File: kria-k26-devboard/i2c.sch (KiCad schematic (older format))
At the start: 10 parts

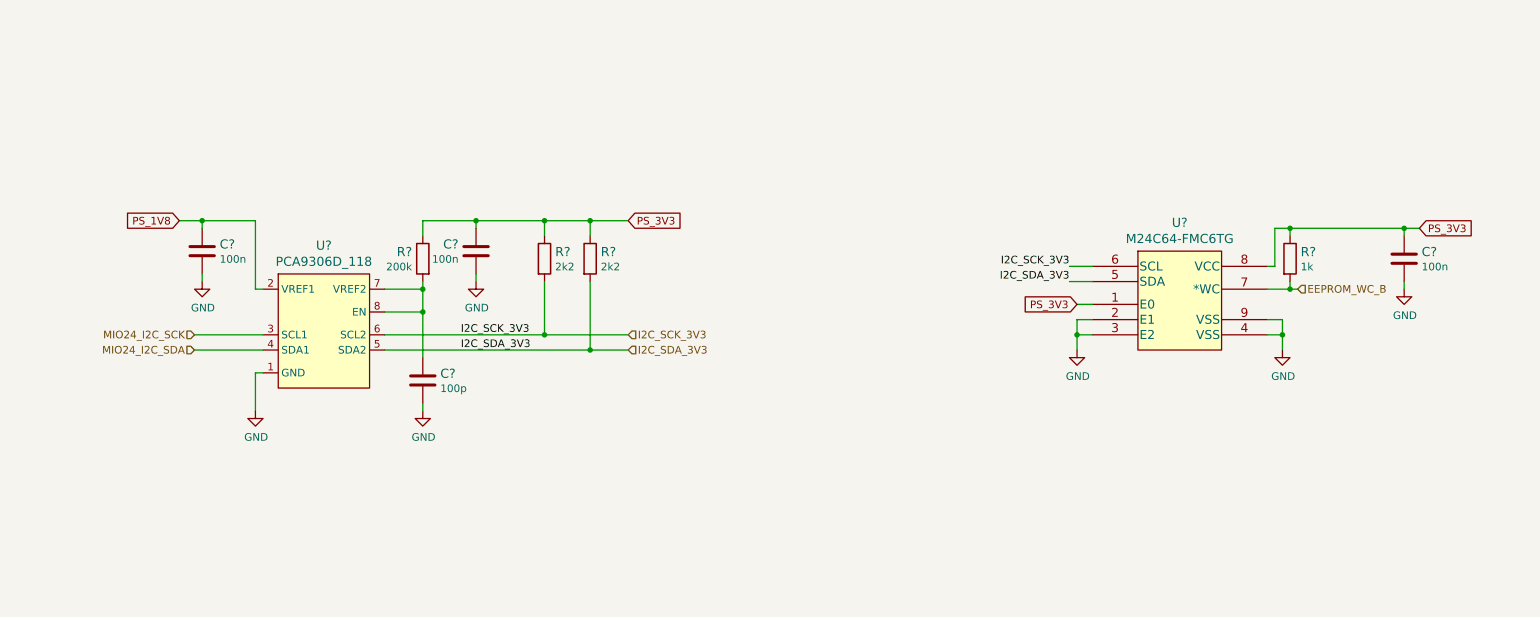
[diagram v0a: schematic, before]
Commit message: Added second ETH interface, connect POE PSE
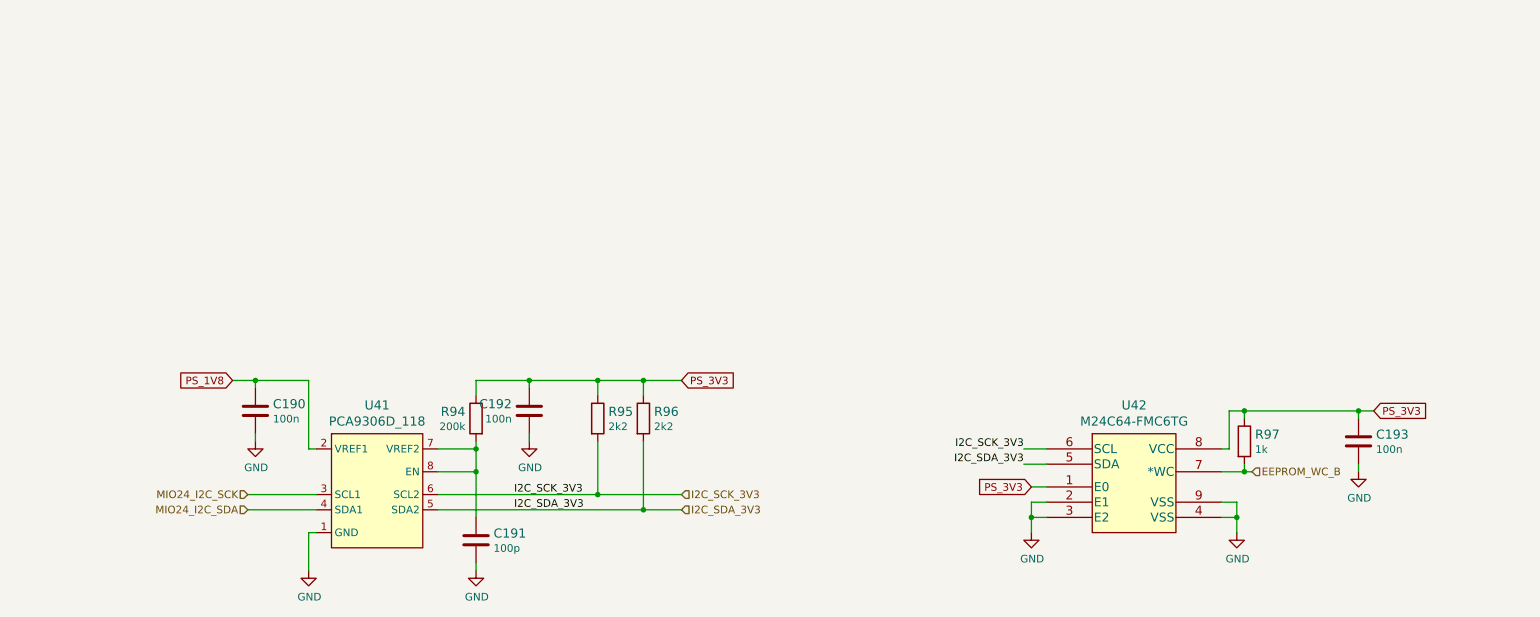
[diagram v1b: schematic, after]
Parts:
- gave numbers to parts that had none: 10
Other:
- moved on the sheet: C190, C191, C192, C193, R94, R95, R96, R97, U41, U42

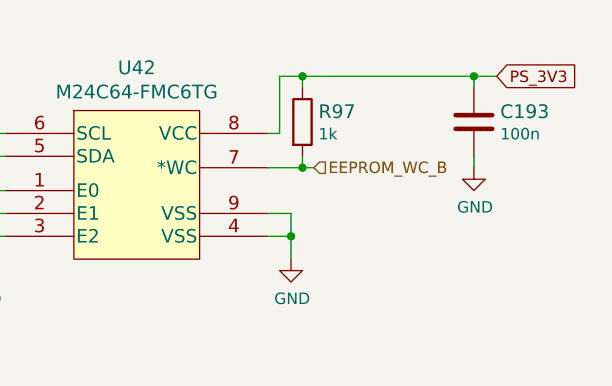
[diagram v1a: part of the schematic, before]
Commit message: Fixes on Reset pagae, progress through clock sheet
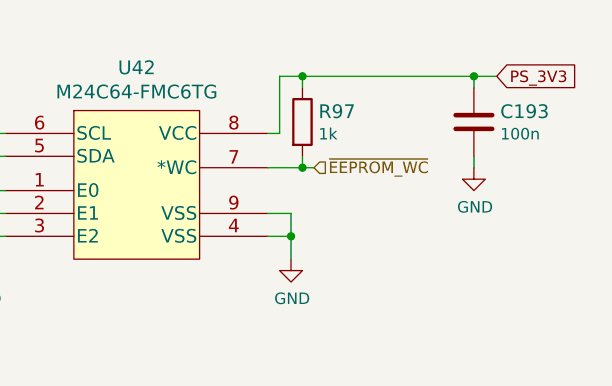
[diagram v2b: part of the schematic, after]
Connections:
- net EEPROM_WC_B renamed ~EEPROM_WC
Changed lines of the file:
@@
 $Descr A4 11693 8268
 encoding utf-8
-Sheet 18 19
+Sheet 16 19
 Title ""
 Date ""
@@
 Connection ~ 8700 3550
 Text HLabel 8750 3550 2    50   Input ~ 0
-EEPROM_WC_B
+~EEPROM_WC
 $EndSCHEMATC

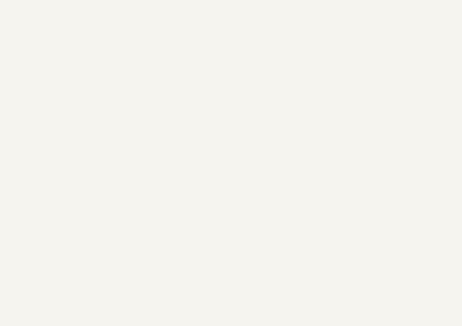
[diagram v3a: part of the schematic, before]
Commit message: Finished tidying up the schematic
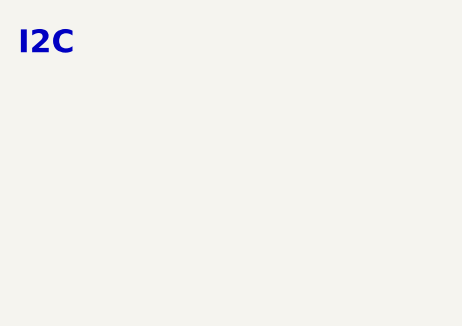
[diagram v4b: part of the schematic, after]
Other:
- note added: "I2C"
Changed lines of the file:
@@
 $Descr A4 11693 8268
 encoding utf-8
-Sheet 15 19
+Sheet 7 19
 Title ""
 Date ""
@@
 Text HLabel 8750 3550 2    50   Input ~ 0
 ~EEPROM_WC
+Text Notes 600  700  0    100  ~ 20
+I2C
 $EndSCHEMATC

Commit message: Progress in PCB placement
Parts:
- renumbered C190 to C35, C191 to C36, C192 to C37, C193 to C38, R94 to R35, R95 to R36, R96 to R37, R97 to R38, U41 to U10, U42 to U11
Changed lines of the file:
@@
 $EndDescr
 $Comp
-L antmicroMemory:M24C64-FMC6TG U42
+L antmicroMemory:M24C64-FMC6TG U11
 U 1 1 63AA3244
 P 7400 3500
-F 0 "U42" H 7975 3887 60  0000 C CNN
+F 0 "U11" H 7975 3887 60  0000 C CNN
 F 1 "M24C64-FMC6TG" H 7975 3781 60  0000 C CNN
 F 2 "antmicro-footprints:STM_UFDFPN8DFN8_2X3" H 7950 3740 60  0001 C CNN
@@
 $EndComp
 $Comp
-L antmicroLogicTranslatorsLevelShifters:PCA9306D_118 U41
+L antmicroLogicTranslatorsLevelShifters:PCA9306D_118 U10
 U 1 1 63AA40DC
 P 3000 3650
-F 0 "U41" H 3000 4187 60  0000 C CNN
+F 0 "U10" H 3000 4187 60  0000 C CNN
 F 1 "PCA9306D_118" H 3000 4081 60  0000 C CNN
 F 2 "antmicro-footprints:SOIC-8_W3.9mm" H 2200 3100 60  0001 L CNN
@@
 PS_1V8
 $Comp
-L antmicroCapacitors0402:C_100n_0402 C190
+L antmicroCapacitors0402:C_100n_0402 C35
 U 1 1 63AA8FCC
 P 2200 3150
-F 0 "C190" H 2315 3195 60  0000 L CNN
+F 0 "C35" H 2315 3195 60  0000 L CNN
 F 1 "C_100n_0402" H 2200 3000 60  0001 C CNN
 F 2 "antmicro-footprints:0402-cap" H 2400 3350 60  0001 L CNN
@@
 Connection ~ 2200 2950
 $Comp
-L power:GND #PWR0322
+L power:GND #PWR055
 U 1 1 63AAAA5A
 P 2200 3350
-F 0 "#PWR0322" H 2200 3100 50  0001 C CNN
+F 0 "#PWR055" H 2200 3100 50  0001 C CNN
 F 1 "GND" H 2205 3177 50  0000 C CNN
 F 2 "" H 2200 3350 50  0001 C CNN
@@
 PS_3V3
 $Comp
-L antmicroCapacitors0402:C_100n_0402 C192
+L antmicroCapacitors0402:C_100n_0402 C37
 U 1 1 63AACD61
 P 4000 3150
-F 0 "C192" H 4115 3195 60  0000 L CNN
+F 0 "C37" H 4115 3195 60  0000 L CNN
 F 1 "C_100n_0402" H 4000 3000 60  0001 C CNN
 F 2 "antmicro-footprints:0402-cap" H 4200 3350 60  0001 L CNN
@@
 Connection ~ 4000 2950
 $Comp
-L power:GND #PWR0323
+L power:GND #PWR058
 U 1 1 63AAF48D
 P 4000 3350
-F 0 "#PWR0323" H 4000 3100 50  0001 C CNN
+F 0 "#PWR058" H 4000 3100 50  0001 C CNN
 F 1 "GND" H 4005 3177 50  0000 C CNN
 F 2 "" H 4000 3350 50  0001 C CNN
@@
 	4000 3350 4000 3300
 $Comp
-L antmicroResistors0402:R_200k_0402 R94
+L antmicroResistors0402:R_200k_0402 R35
 U 1 1 63AB0E0E
 P 3650 3200
-F 0 "R94" V 3605 3270 60  0000 L CNN
+F 0 "R35" V 3605 3270 60  0000 L CNN
 F 1 "R_200k_0402" H 3650 3050 60  0001 C CNN
 F 2 "antmicro-footprints:0402-res" H 3850 3400 60  0001 L CNN
@@
 	2550 3950 2550 4200
 $Comp
-L power:GND #PWR0324
+L power:GND #PWR056
 U 1 1 63AB6E2C
 P 2550 4200
-F 0 "#PWR0324" H 2550 3950 50  0001 C CNN
+F 0 "#PWR056" H 2550 3950 50  0001 C CNN
 F 1 "GND" H 2555 4027 50  0000 C CNN
 F 2 "" H 2550 4200 50  0001 C CNN
@@
 $EndComp
 $Comp
-L antmicroCapacitors0402:C_100p_0402 C191
+L antmicroCapacitors0402:C_100p_0402 C36
 U 1 1 63AB8096
 P 3650 4000
-F 0 "C191" H 3765 4045 60  0000 L CNN
+F 0 "C36" H 3765 4045 60  0000 L CNN
 F 1 "C_100p_0402" H 3650 3850 60  0001 C CNN
 F 2 "antmicro-footprints:0402-cap" H 3850 4200 60  0001 L CNN
@@
 	7250 3500 7400 3500
 $Comp
-L antmicroResistors0402:R_2k2_0402 R95
+L antmicroResistors0402:R_2k2_0402 R36
 U 1 1 63AC2DF3
 P 4450 3200
-F 0 "R95" V 4405 3270 60  0000 L CNN
+F 0 "R36" V 4405 3270 60  0000 L CNN
 F 1 "R_2k2_0402" H 4450 3050 60  0001 C CNN
 F 2 "antmicro-footprints:0402-res" H 4650 3400 60  0001 L CNN
@@
 $EndComp
 $Comp
-L antmicroResistors0402:R_2k2_0402 R96
+L antmicroResistors0402:R_2k2_0402 R37
 U 1 1 63AC330F
 P 4750 3200
-F 0 "R96" V 4705 3270 60  0000 L CNN
+F 0 "R37" V 4705 3270 60  0000 L CNN
 F 1 "R_2k2_0402" H 4750 3050 60  0001 C CNN
 F 2 "antmicro-footprints:0402-res" H 4950 3400 60  0001 L CNN
@@
 Connection ~ 8650 3850
 $Comp
-L power:GND #PWR0325
+L power:GND #PWR057
 U 1 1 63AB8856
 P 3650 4200
-F 0 "#PWR0325" H 3650 3950 50  0001 C CNN
+F 0 "#PWR057" H 3650 3950 50  0001 C CNN
 F 1 "GND" H 3655 4027 50  0000 C CNN
 F 2 "" H 3650 4200 50  0001 C CNN
@@
 $EndComp
 $Comp
-L power:GND #PWR0326
+L power:GND #PWR060
 U 1 1 63AD94E4
 P 8650 3950
-F 0 "#PWR0326" H 8650 3700 50  0001 C CNN
+F 0 "#PWR060" H 8650 3700 50  0001 C CNN
 F 1 "GND" H 8655 3777 50  0000 C CNN
 F 2 "" H 8650 3950 50  0001 C CNN
@@
 	7300 3850 7300 3950
 $Comp
-L power:GND #PWR0327
+L power:GND #PWR059
 U 1 1 63ADADB2
 P 7300 3950
-F 0 "#PWR0327" H 7300 3700 50  0001 C CNN
+F 0 "#PWR059" H 7300 3700 50  0001 C CNN
 F 1 "GND" H 7305 3777 50  0000 C CNN
 F 2 "" H 7300 3950 50  0001 C CNN
@@
 	8700 3150 8700 3200
 $Comp
-L antmicroCapacitors0402:C_100n_0402 C193
+L antmicroCapacitors0402:C_100n_0402 C38
 U 1 1 63AE0E22
 P 9450 3350
-F 0 "C193" H 9335 3305 60  0000 R CNN
+F 0 "C38" H 9335 3305 60  0000 R CNN
 F 1 "C_100n_0402" H 9450 3200 60  0001 C CNN
 F 2 "antmicro-footprints:0402-cap" H 9650 3550 60  0001 L CNN
@@
 	9450 3200 9450 3150
 $Comp
-L power:GND #PWR0328
+L power:GND #PWR061
 U 1 1 63AE2AFC
 P 9450 3550
-F 0 "#PWR0328" H 9450 3300 50  0001 C CNN
+F 0 "#PWR061" H 9450 3300 50  0001 C CNN
 F 1 "GND" H 9455 3377 50  0000 C CNN
 F 2 "" H 9450 3550 50  0001 C CNN
@@
 	8550 3550 8700 3550
 $Comp
-L antmicroResistors0402:R_1k_0402 R97
+L antmicroResistors0402:R_1k_0402 R38
 U 1 1 63ADC97D
 P 8700 3350
-F 0 "R97" V 8655 3420 60  0000 L CNN
+F 0 "R38" V 8655 3420 60  0000 L CNN
 F 1 "R_1k_0402" H 8700 3200 60  0001 C CNN
 F 2 "antmicro-footprints:0402-res" H 8900 3550 60  0001 L CNN

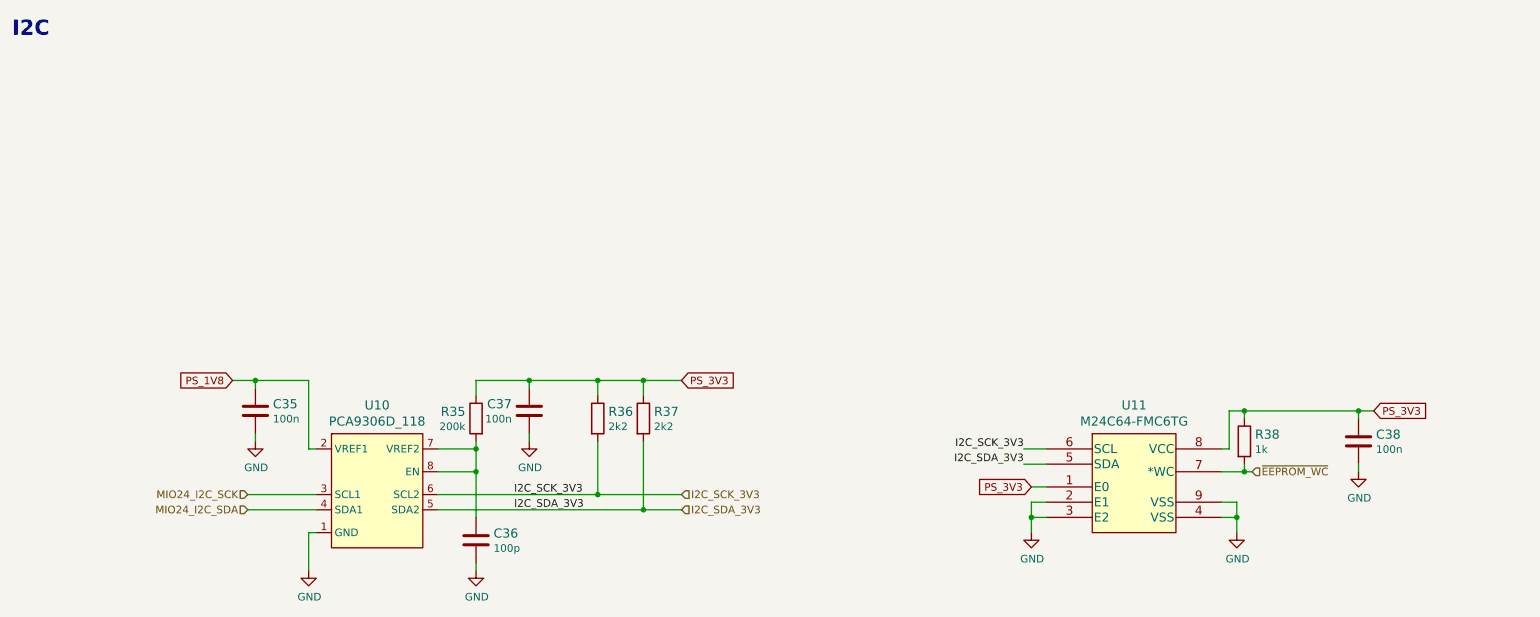
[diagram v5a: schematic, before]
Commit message: Fixed missing USB - M2 connection, finishing touches of PCB
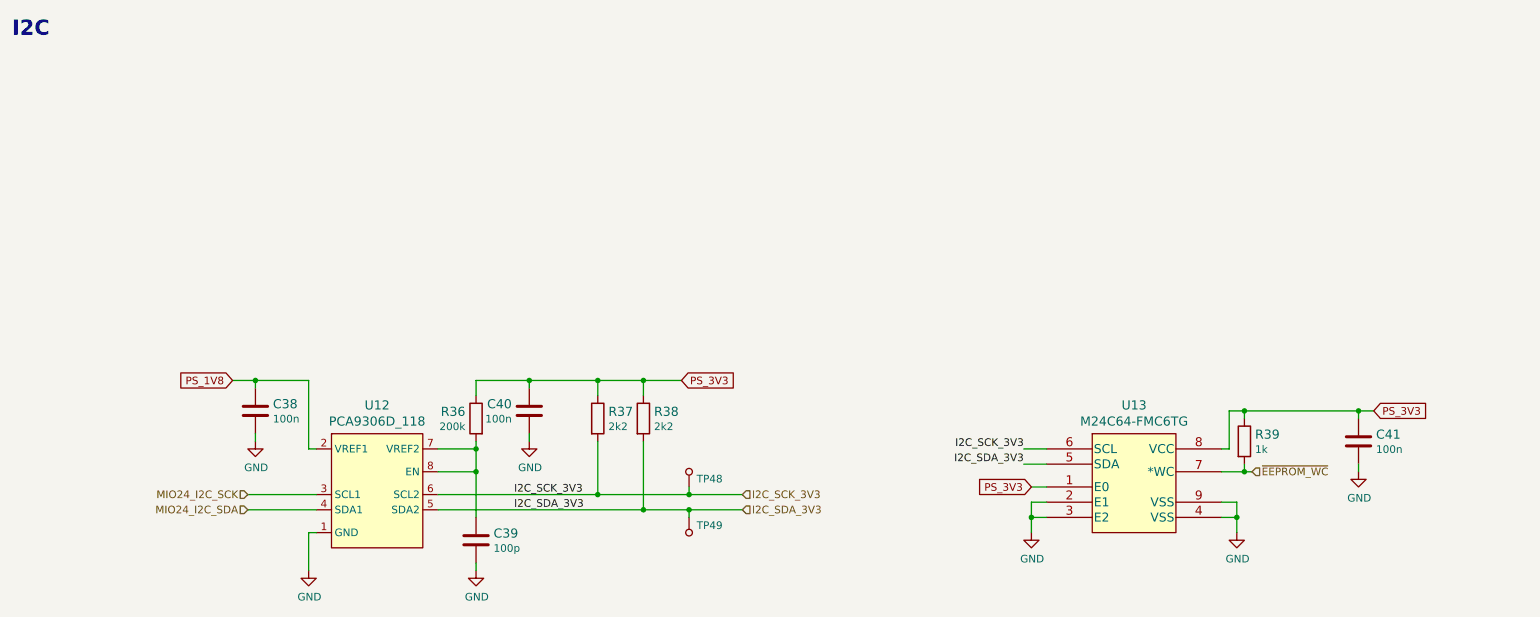
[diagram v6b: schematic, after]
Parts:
- added TP48, TP49: TP_SMD_0_75MM, antmicro-footprints:Testpoint_smd_0_75mm, symbol antmicroTestPoints:TP_SMD_0_75MM
- renumbered C35 to C38, C36 to C39, C37 to C40, C38 to C41, R35 to R36, R36 to R37, R37 to R38, R38 to R39, U10 to U12, U11 to U13
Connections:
- net I2C_SCK_3V3: now also TP48.1
- net I2C_SDA_3V3: now also TP49.1
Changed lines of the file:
@@
 $EndDescr
 $Comp
-L antmicroMemory:M24C64-FMC6TG U11
+L antmicroMemory:M24C64-FMC6TG U13
 U 1 1 63AA3244
 P 7400 3500
-F 0 "U11" H 7975 3887 60  0000 C CNN
+F 0 "U13" H 7975 3887 60  0000 C CNN
 F 1 "M24C64-FMC6TG" H 7975 3781 60  0000 C CNN
 F 2 "antmicro-footprints:STM_UFDFPN8DFN8_2X3" H 7950 3740 60  0001 C CNN
@@
 $EndComp
 $Comp
-L antmicroLogicTranslatorsLevelShifters:PCA9306D_118 U10
+L antmicroLogicTranslatorsLevelShifters:PCA9306D_118 U12
 U 1 1 63AA40DC
 P 3000 3650
-F 0 "U10" H 3000 4187 60  0000 C CNN
+F 0 "U12" H 3000 4187 60  0000 C CNN
 F 1 "PCA9306D_118" H 3000 4081 60  0000 C CNN
 F 2 "antmicro-footprints:SOIC-8_W3.9mm" H 2200 3100 60  0001 L CNN
@@
 PS_1V8
 $Comp
-L antmicroCapacitors0402:C_100n_0402 C35
+L antmicroCapacitors0402:C_100n_0402 C38
 U 1 1 63AA8FCC
 P 2200 3150
-F 0 "C35" H 2315 3195 60  0000 L CNN
+F 0 "C38" H 2315 3195 60  0000 L CNN
 F 1 "C_100n_0402" H 2200 3000 60  0001 C CNN
 F 2 "antmicro-footprints:0402-cap" H 2400 3350 60  0001 L CNN
@@
 Connection ~ 2200 2950
 $Comp
-L power:GND #PWR055
+L power:GND #PWR061
 U 1 1 63AAAA5A
 P 2200 3350
-F 0 "#PWR055" H 2200 3100 50  0001 C CNN
+F 0 "#PWR061" H 2200 3100 50  0001 C CNN
 F 1 "GND" H 2205 3177 50  0000 C CNN
 F 2 "" H 2200 3350 50  0001 C CNN
@@
 PS_3V3
 $Comp
-L antmicroCapacitors0402:C_100n_0402 C37
+L antmicroCapacitors0402:C_100n_0402 C40
 U 1 1 63AACD61
 P 4000 3150
-F 0 "C37" H 4115 3195 60  0000 L CNN
+F 0 "C40" H 4115 3195 60  0000 L CNN
 F 1 "C_100n_0402" H 4000 3000 60  0001 C CNN
 F 2 "antmicro-footprints:0402-cap" H 4200 3350 60  0001 L CNN
@@
 Connection ~ 4000 2950
 $Comp
-L power:GND #PWR058
+L power:GND #PWR064
 U 1 1 63AAF48D
 P 4000 3350
-F 0 "#PWR058" H 4000 3100 50  0001 C CNN
+F 0 "#PWR064" H 4000 3100 50  0001 C CNN
 F 1 "GND" H 4005 3177 50  0000 C CNN
 F 2 "" H 4000 3350 50  0001 C CNN
@@
 	4000 3350 4000 3300
 $Comp
-L antmicroResistors0402:R_200k_0402 R35
+L antmicroResistors0402:R_200k_0402 R36
 U 1 1 63AB0E0E
 P 3650 3200
-F 0 "R35" V 3605 3270 60  0000 L CNN
+F 0 "R36" V 3605 3270 60  0000 L CNN
 F 1 "R_200k_0402" H 3650 3050 60  0001 C CNN
 F 2 "antmicro-footprints:0402-res" H 3850 3400 60  0001 L CNN
@@
 	2550 3950 2550 4200
 $Comp
-L power:GND #PWR056
+L power:GND #PWR062
 U 1 1 63AB6E2C
 P 2550 4200
-F 0 "#PWR056" H 2550 3950 50  0001 C CNN
+F 0 "#PWR062" H 2550 3950 50  0001 C CNN
 F 1 "GND" H 2555 4027 50  0000 C CNN
 F 2 "" H 2550 4200 50  0001 C CNN
@@
 $EndComp
 $Comp
-L antmicroCapacitors0402:C_100p_0402 C36
+L antmicroCapacitors0402:C_100p_0402 C39
 U 1 1 63AB8096
 P 3650 4000
-F 0 "C36" H 3765 4045 60  0000 L CNN
+F 0 "C39" H 3765 4045 60  0000 L CNN
 F 1 "C_100p_0402" H 3650 3850 60  0001 C CNN
 F 2 "antmicro-footprints:0402-cap" H 3850 4200 60  0001 L CNN
@@
 Wire Wire Line
 	3400 3700 4450 3700
-Text HLabel 5000 3800 2    50   Input ~ 0
+Text HLabel 5400 3800 2    50   Input ~ 0
 I2C_SDA_3V3
-Text HLabel 5000 3700 2    50   Input ~ 0
+Text HLabel 5400 3700 2    50   Input ~ 0
 I2C_SCK_3V3
 Text Label 3900 3700 0    50   ~ 0
@@
 	7250 3500 7400 3500
 $Comp
-L antmicroResistors0402:R_2k2_0402 R36
+L antmicroResistors0402:R_2k2_0402 R37
 U 1 1 63AC2DF3
 P 4450 3200
-F 0 "R36" V 4405 3270 60  0000 L CNN
+F 0 "R37" V 4405 3270 60  0000 L CNN
 F 1 "R_2k2_0402" H 4450 3050 60  0001 C CNN
 F 2 "antmicro-footprints:0402-res" H 4650 3400 60  0001 L CNN
@@
 $EndComp
 $Comp
-L antmicroResistors0402:R_2k2_0402 R37
+L antmicroResistors0402:R_2k2_0402 R38
 U 1 1 63AC330F
 P 4750 3200
-F 0 "R37" V 4705 3270 60  0000 L CNN
+F 0 "R38" V 4705 3270 60  0000 L CNN
 F 1 "R_2k2_0402" H 4750 3050 60  0001 C CNN
 F 2 "antmicro-footprints:0402-res" H 4950 3400 60  0001 L CNN
@@
 Connection ~ 4450 3700
 Wire Wire Line
-	4450 3700 5000 3700
+	4450 3700 5050 3700
 Wire Wire Line
 	4750 3350 4750 3800
@@
 Connection ~ 4750 3800
 Wire Wire Line
-	4750 3800 5000 3800
+	4750 3800 5050 3800
 Connection ~ 4750 2950
 Text GLabel 9550 3150 2    50   Input ~ 0
@@
 Connection ~ 8650 3850
 $Comp
-L power:GND #PWR057
+L power:GND #PWR063
 U 1 1 63AB8856
 P 3650 4200
-F 0 "#PWR057" H 3650 3950 50  0001 C CNN
+F 0 "#PWR063" H 3650 3950 50  0001 C CNN
 F 1 "GND" H 3655 4027 50  0000 C CNN
 F 2 "" H 3650 4200 50  0001 C CNN
@@
 $EndComp
 $Comp
-L power:GND #PWR060
+L power:GND #PWR066
 U 1 1 63AD94E4
 P 8650 3950
-F 0 "#PWR060" H 8650 3700 50  0001 C CNN
+F 0 "#PWR066" H 8650 3700 50  0001 C CNN
 F 1 "GND" H 8655 3777 50  0000 C CNN
 F 2 "" H 8650 3950 50  0001 C CNN
@@
 	7300 3850 7300 3950
 $Comp
-L power:GND #PWR059
+L power:GND #PWR065
 U 1 1 63ADADB2
 P 7300 3950
-F 0 "#PWR059" H 7300 3700 50  0001 C CNN
+F 0 "#PWR065" H 7300 3700 50  0001 C CNN
 F 1 "GND" H 7305 3777 50  0000 C CNN
 F 2 "" H 7300 3950 50  0001 C CNN
@@
 	8700 3150 8700 3200
 $Comp
-L antmicroCapacitors0402:C_100n_0402 C38
+L antmicroCapacitors0402:C_100n_0402 C41
 U 1 1 63AE0E22
 P 9450 3350
-F 0 "C38" H 9335 3305 60  0000 R CNN
+F 0 "C41" H 9335 3305 60  0000 R CNN
 F 1 "C_100n_0402" H 9450 3200 60  0001 C CNN
 F 2 "antmicro-footprints:0402-cap" H 9650 3550 60  0001 L CNN
@@
 	9450 3200 9450 3150
 $Comp
-L power:GND #PWR061
+L power:GND #PWR067
 U 1 1 63AE2AFC
 P 9450 3550
-F 0 "#PWR061" H 9450 3300 50  0001 C CNN
+F 0 "#PWR067" H 9450 3300 50  0001 C CNN
 F 1 "GND" H 9455 3377 50  0000 C CNN
 F 2 "" H 9450 3550 50  0001 C CNN
@@
 	8550 3550 8700 3550
 $Comp
-L antmicroResistors0402:R_1k_0402 R38
+L antmicroResistors0402:R_1k_0402 R39
 U 1 1 63ADC97D
 P 8700 3350
-F 0 "R38" V 8655 3420 60  0000 L CNN
+F 0 "R39" V 8655 3420 60  0000 L CNN
 F 1 "R_1k_0402" H 8700 3200 60  0001 C CNN
 F 2 "antmicro-footprints:0402-res" H 8900 3550 60  0001 L CNN
@@
 Text Notes 600  700  0    100  ~ 20
 I2C
+$Comp
+L antmicroTestPoints:TP_SMD_0_75MM TP48
+U 1 1 6292C3A1
+P 5050 3550
+F 0 "TP48" H 5000 3597 50  0000 R CNN
+F 1 "TP_SMD_0_75MM" H 5050 3450 50  0001 C CNN
+F 2 "antmicro-footprints:Testpoint_smd_0_75mm" H 5250 3750 60  0001 L CNN
+F 3 "" H 5250 3850 60  0001 L CNN
+	1    5050 3550
+	-1   0    0    1
+$EndComp
+$Comp
+L antmicroTestPoints:TP_SMD_0_75MM TP49
+U 1 1 6292CCE4
+P 5050 3950
+F 0 "TP49" H 5100 3997 50  0000 L CNN
+F 1 "TP_SMD_0_75MM" H 5050 3850 50  0001 C CNN
+F 2 "antmicro-footprints:Testpoint_smd_0_75mm" H 5250 4150 60  0001 L CNN
+F 3 "" H 5250 4250 60  0001 L CNN
+	1    5050 3950
+	1    0    0    -1
+$EndComp
+Wire Wire Line
+	5050 3850 5050 3800
+Connection ~ 5050 3800
+Wire Wire Line
+	5050 3800 5400 3800
+Wire Wire Line
+	5050 3650 5050 3700
+Connection ~ 5050 3700
+Wire Wire Line
+	5050 3700 5400 3700
 $EndSCHEMATC
